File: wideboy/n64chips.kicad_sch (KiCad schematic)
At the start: 7 parts, among them U1 CIC-NUS, U2 BU9850, U6 PST9140N

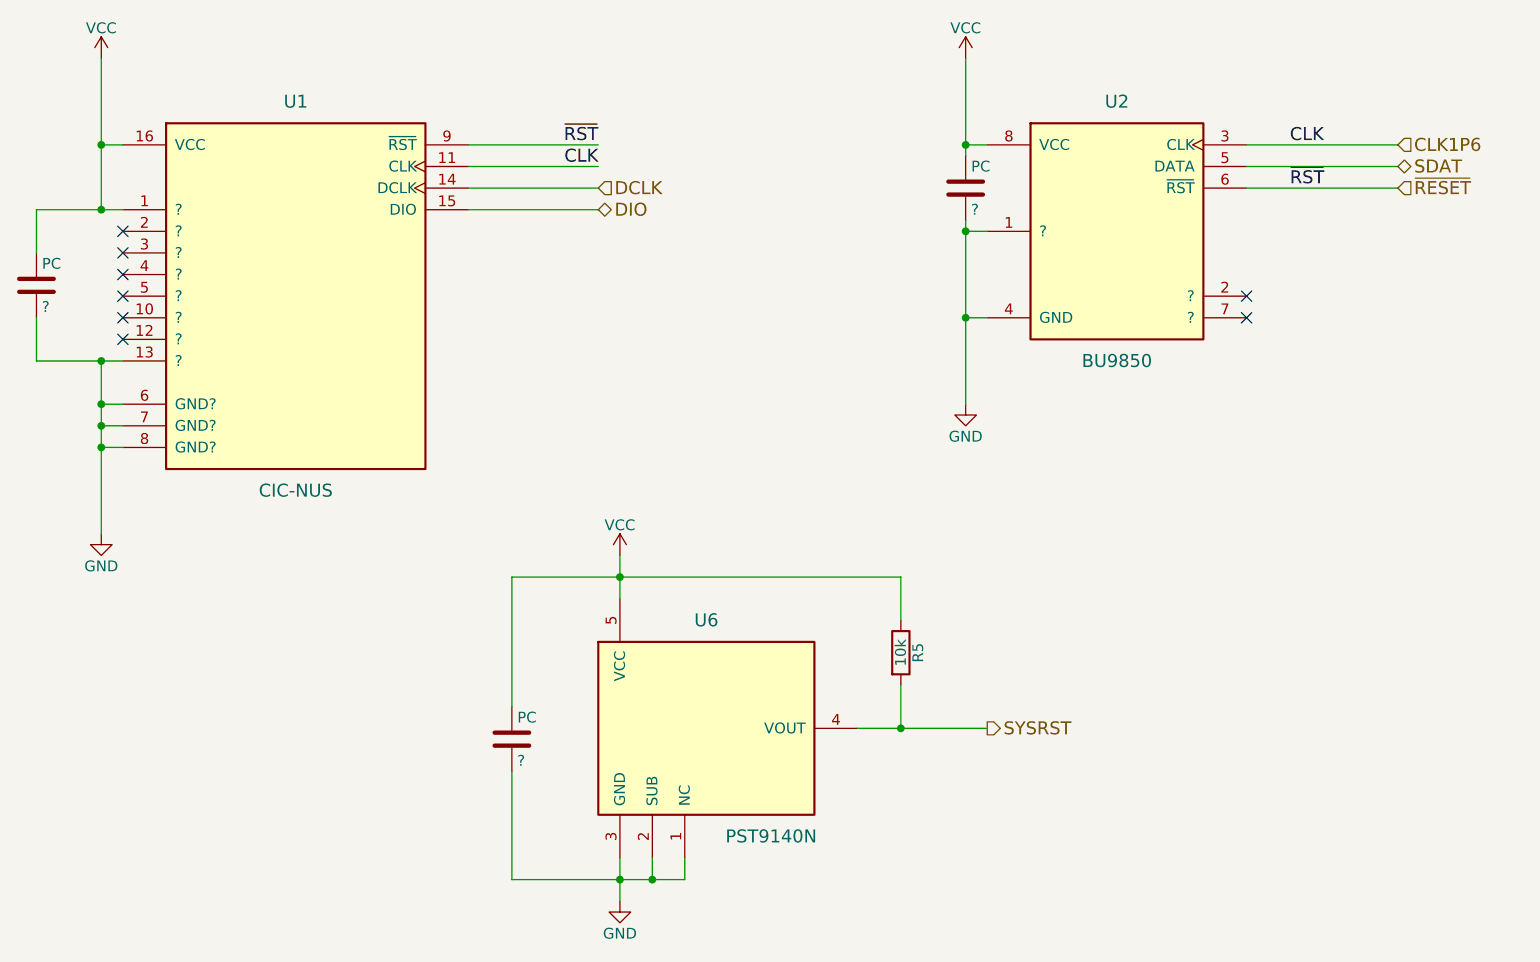
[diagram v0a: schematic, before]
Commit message: Add values for capacitors and diodes
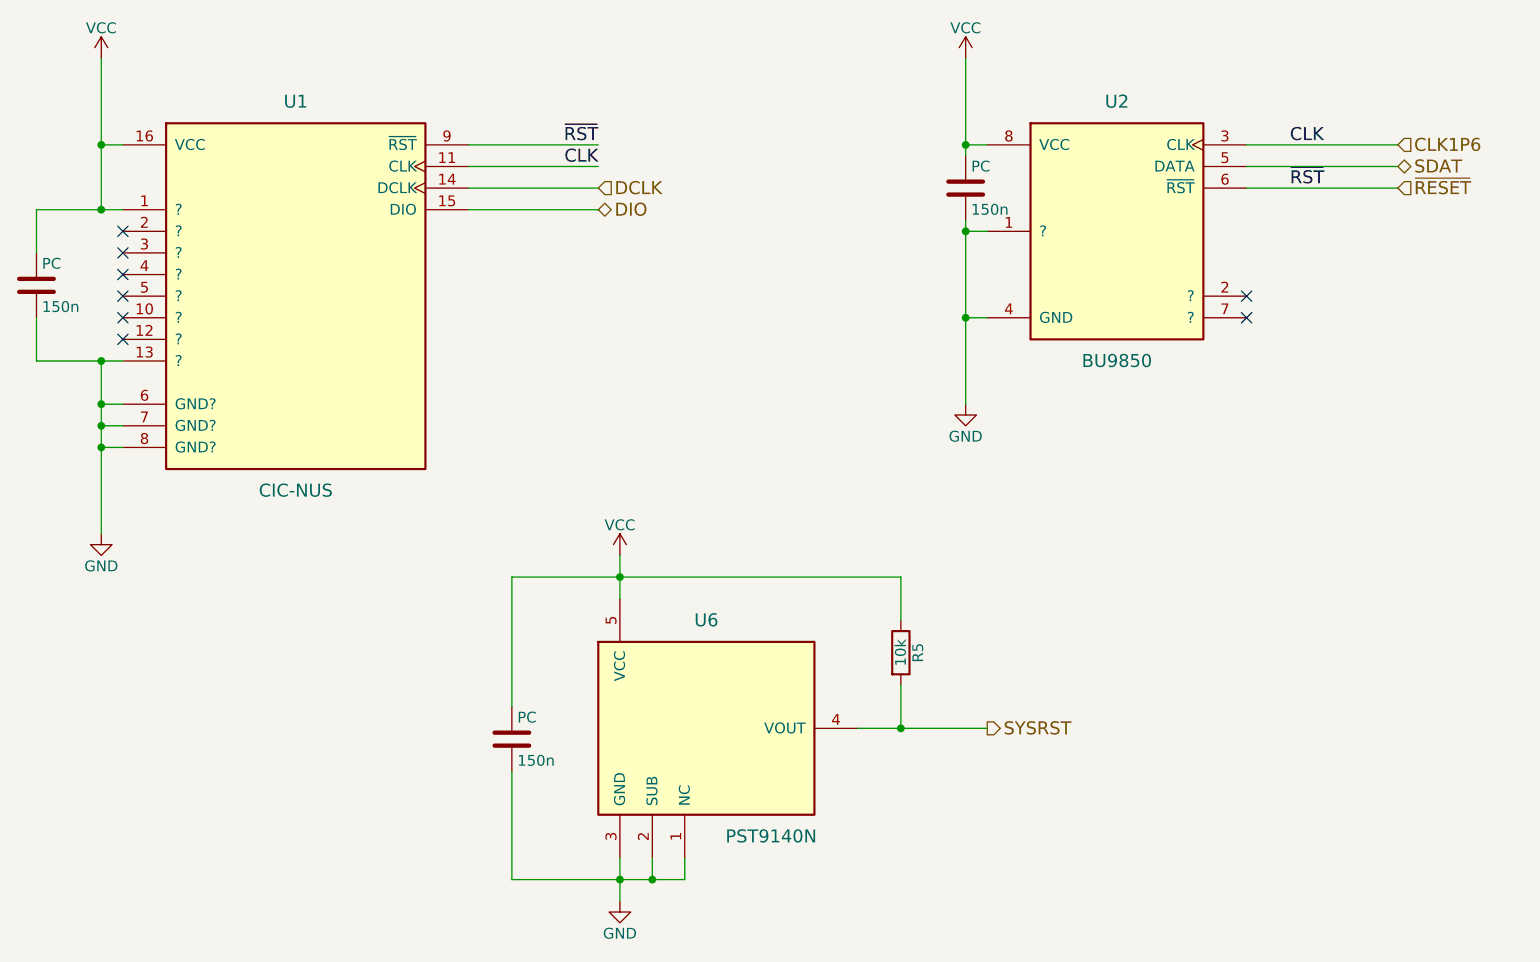
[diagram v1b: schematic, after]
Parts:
- PC: value ? -> 150n
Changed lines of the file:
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@@
 	(title_block
 		(title "Wide-Boy64 AGB")
-		(date "2024-06-20")
-		(rev "2")
+		(date "2024-09-22")
+		(rev "3")
 		(company "CC-BY-SA-4.0 Michael Singer")
 		(comment 1 "https://github.com/msinger/wideboy/")
@@
 			)
 		)
-		(property "Value" "?"
+		(property "Value" "150n"
 			(at 120.015 143.51 0)
 			(effects
@@
 			)
 		)
-		(property "Value" "?"
+		(property "Value" "150n"
 			(at 64.135 90.17 0)
 			(effects
@@
 			)
 		)
-		(property "Value" "?"
+		(property "Value" "150n"
 			(at 173.355 78.74 0)
 			(effects
